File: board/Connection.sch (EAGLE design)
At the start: 44 parts, among them U2 SN65HVD230, U5 ADA4528-1ARMZ-R7, X1 MKDSN1,5/4-5,08

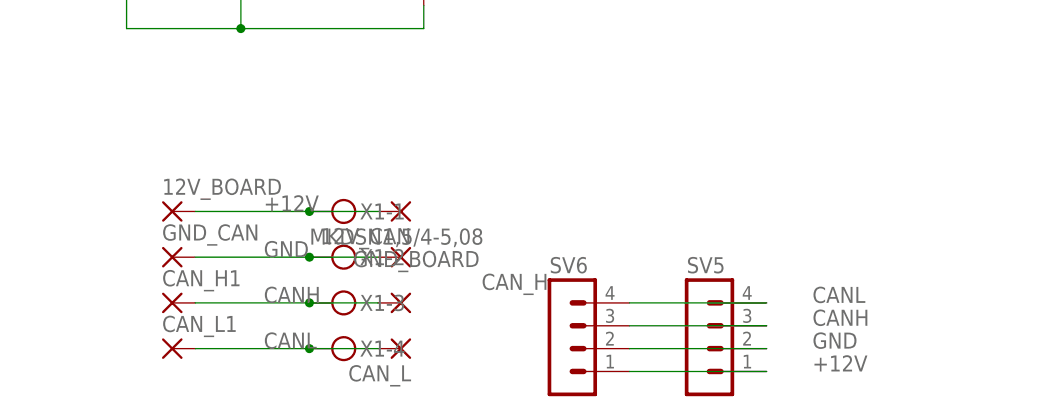
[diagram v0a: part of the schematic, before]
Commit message: Used power terminal
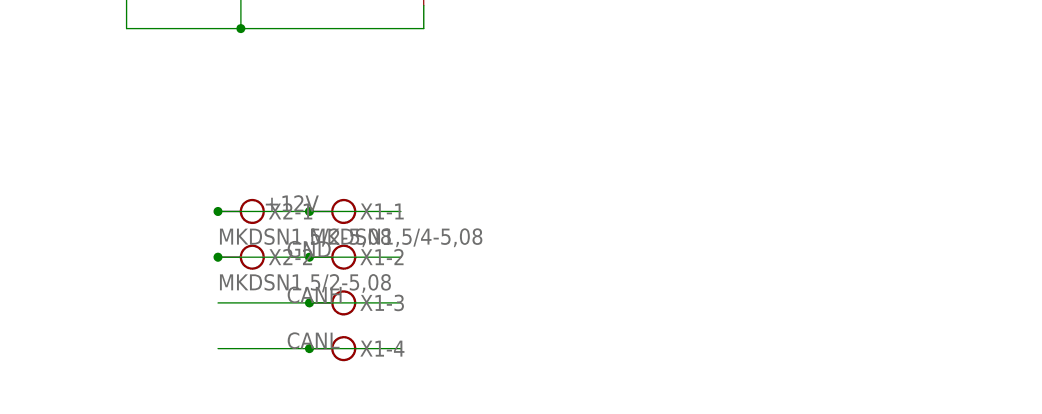
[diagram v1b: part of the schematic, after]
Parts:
- removed 12V_BOARD, 12V_CAN: 12V, wirepad:1,6/0,8
- removed CAN_H, CAN_H1, CAN_L, CAN_L1, GND_BOARD, GND_CAN: (no value), wirepad:1,6/0,8
- removed SV5, SV6: (no value), con-lstb:MA04-1
- added X2: MKDSN1,5/2-5,08, con-phoenix-508:MKDSN1,5/2-5,08
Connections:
- net +12V: now also X2-1.KL; no longer 12V_BOARD.P, 12V_CAN.P, SV5.1, SV6.1
- net CANH: no longer CAN_H.P, CAN_H1.P, SV5.3, SV6.3
- net CANL: no longer CAN_L.P, CAN_L1.P, SV5.4, SV6.4
- net GND: now also X2-2.KL; no longer GND_BOARD.P, GND_CAN.P, SV5.2, SV6.2

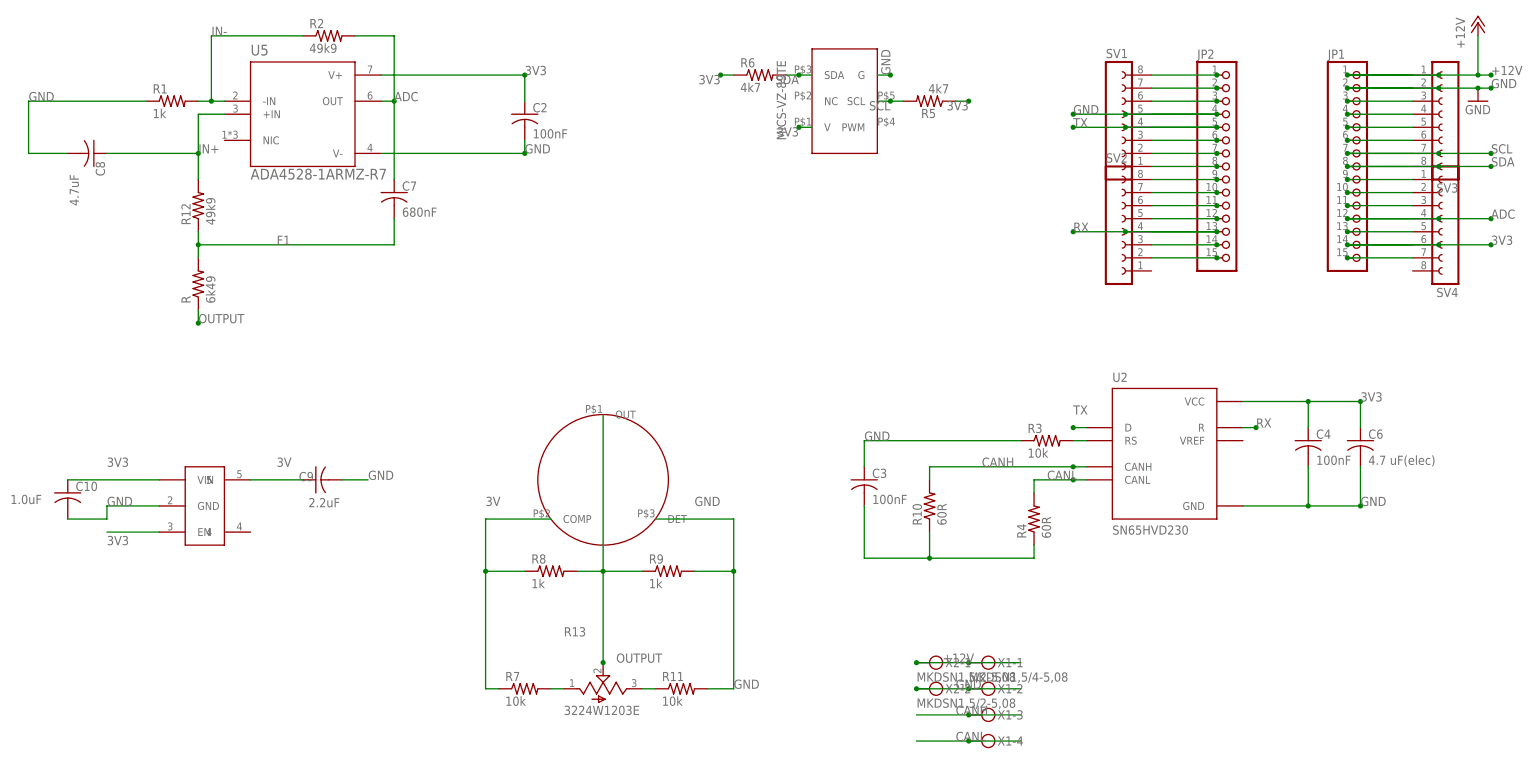
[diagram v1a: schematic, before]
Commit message: Optimized the size of PCB
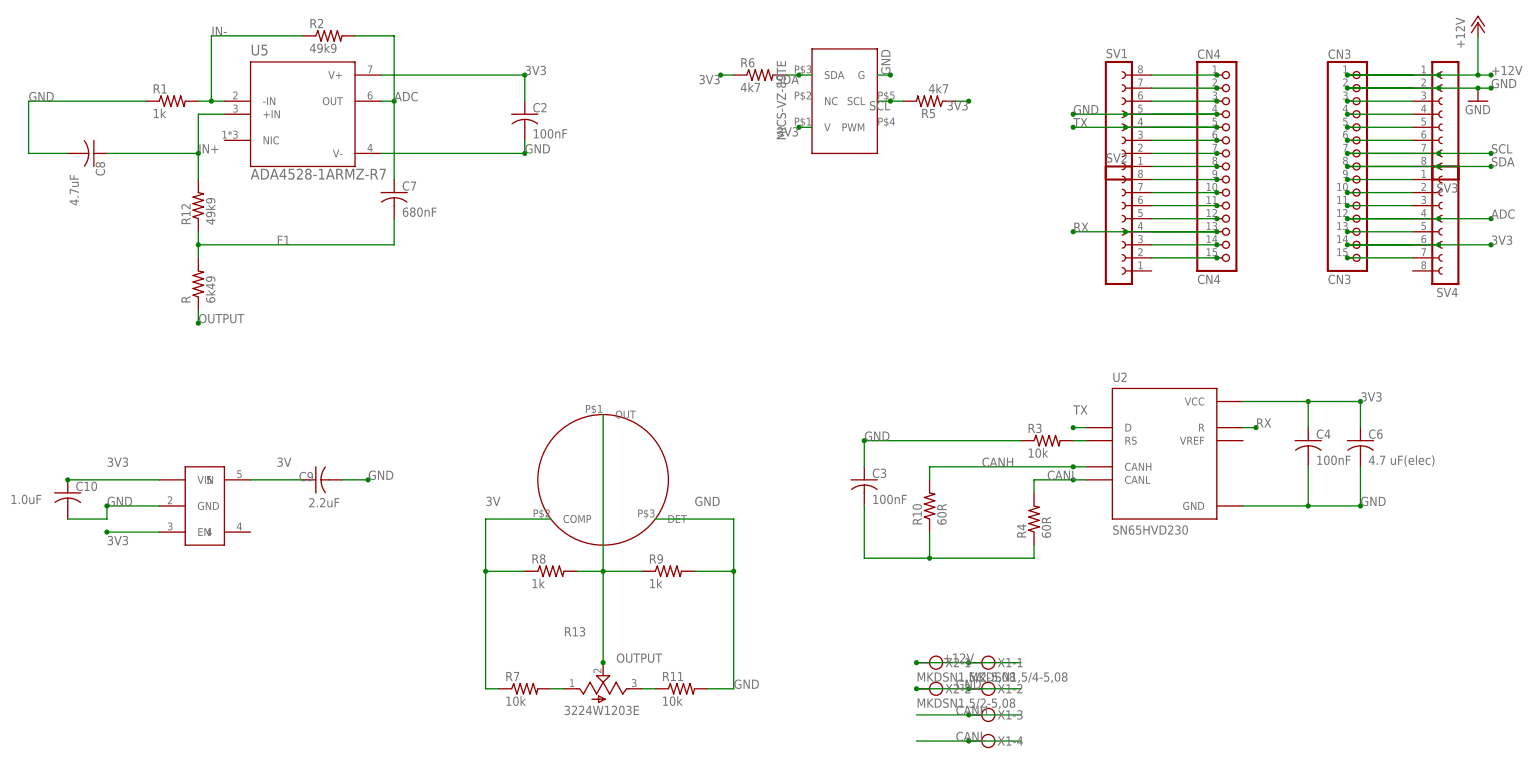
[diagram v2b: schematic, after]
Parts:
- CN3: value (none) -> CN3
- CN4: value (none) -> CN4
- renumbered JP1 to CN3, JP2 to CN4

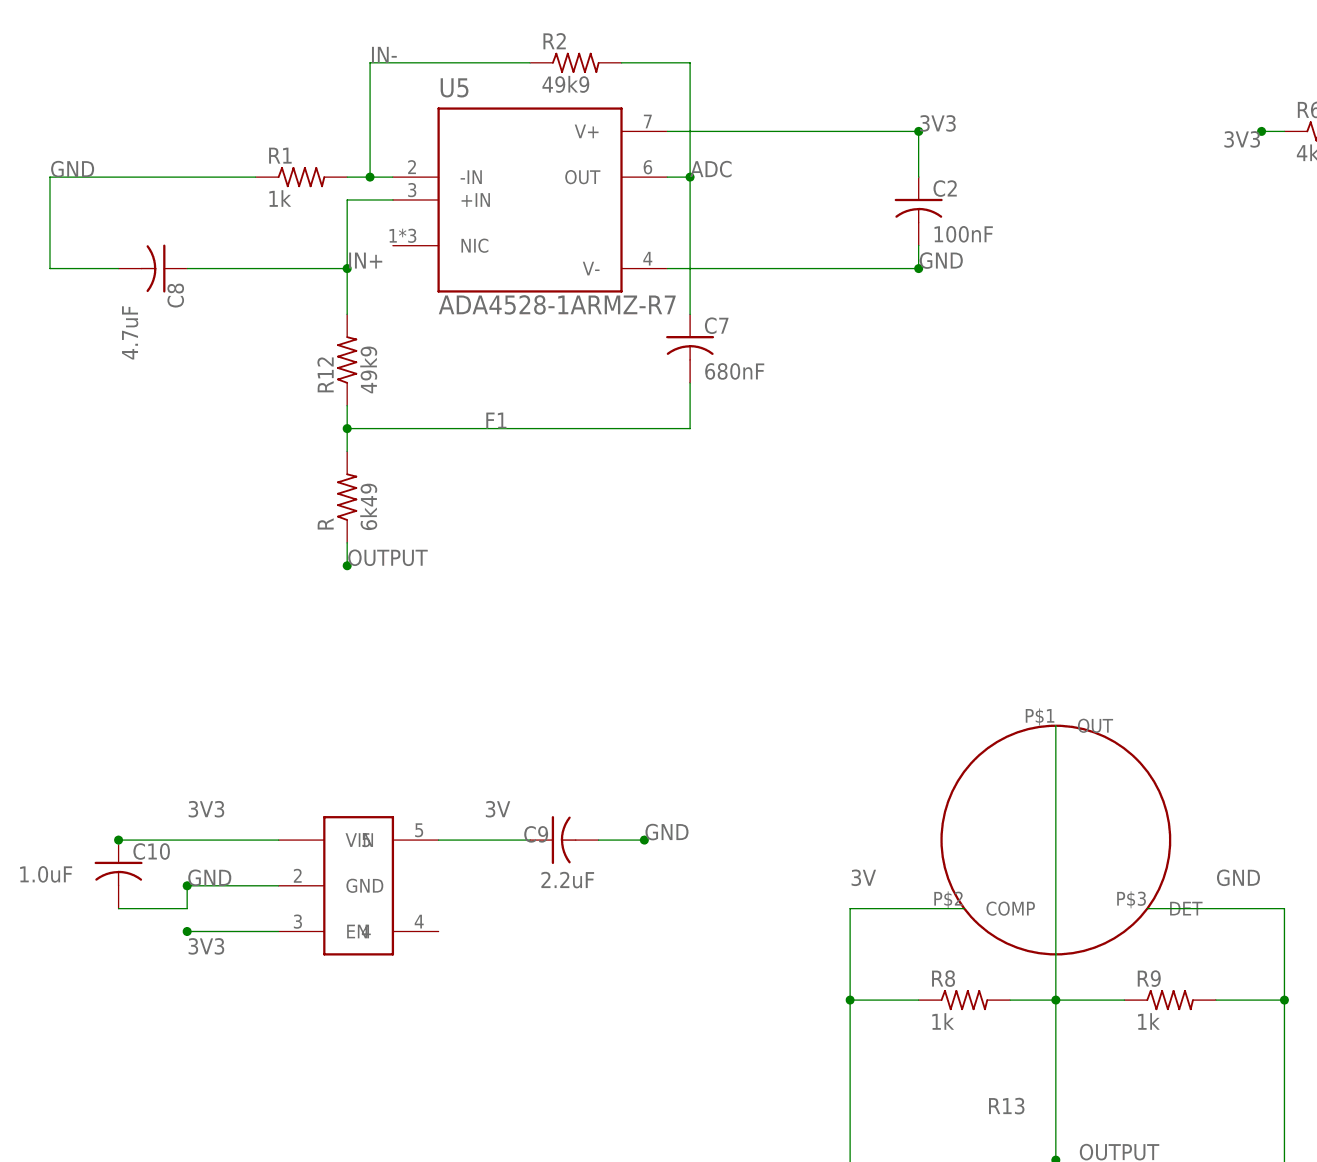
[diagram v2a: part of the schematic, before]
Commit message: Updated the design according to the real connection.
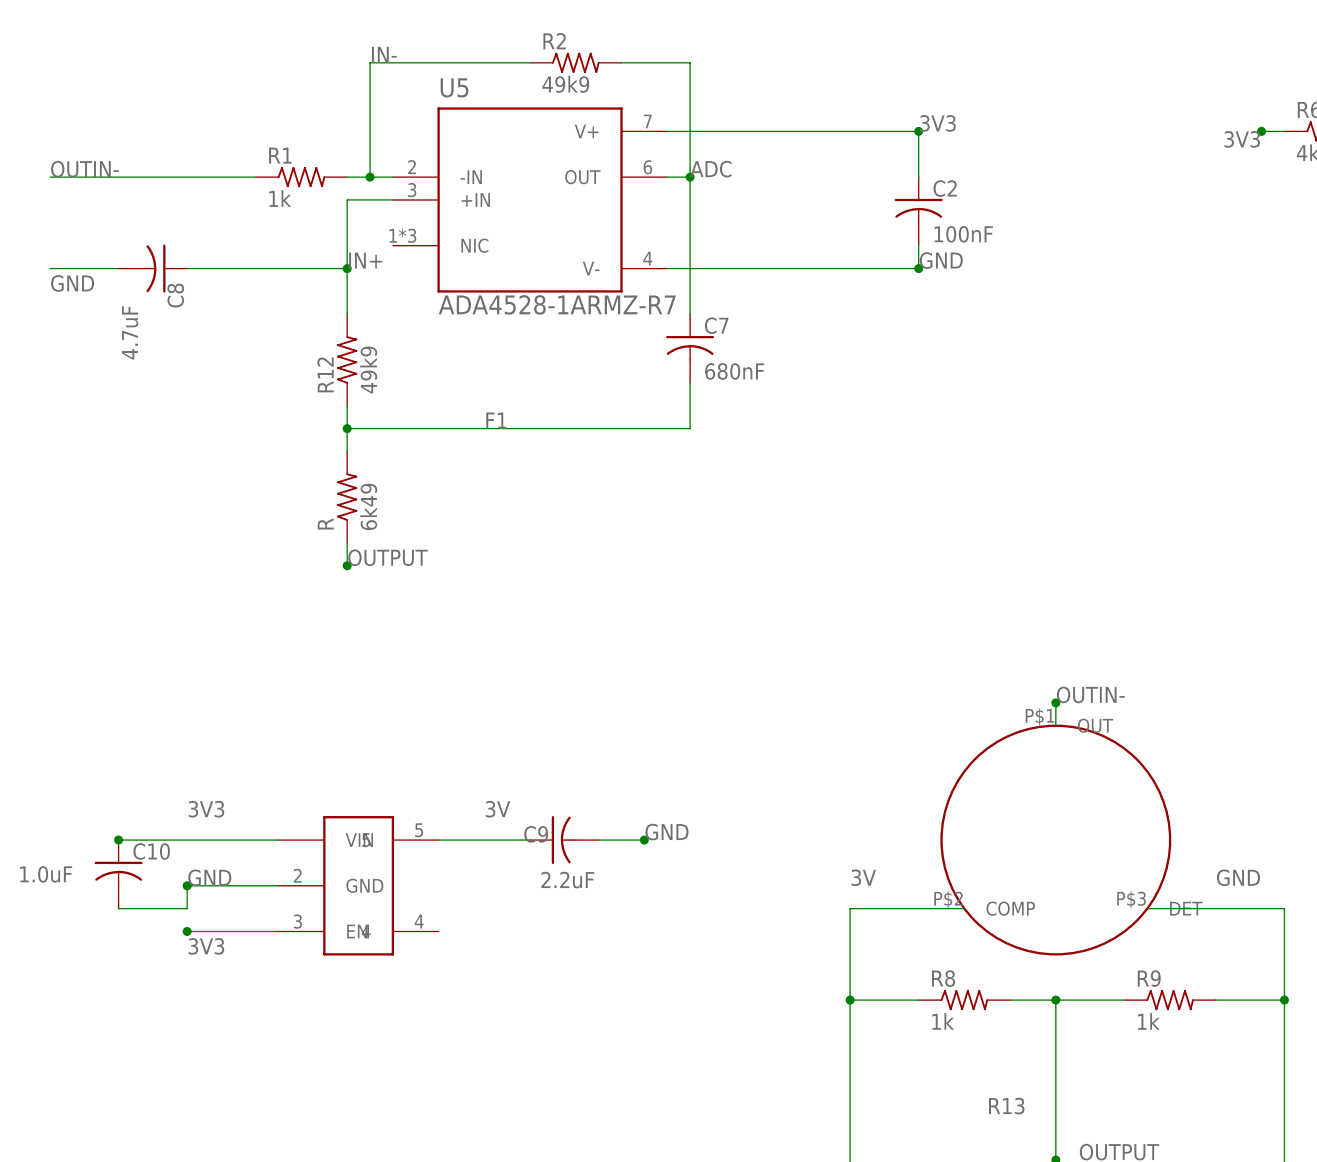
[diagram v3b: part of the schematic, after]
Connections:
- new net OUTIN-: R1.1, U$1.OUT
- net GND: no longer R1.1
- net OUTPUT: no longer U$1.OUT
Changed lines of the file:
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@@
-</segment>
-<segment>
-<pinref part="R1" gate="G$1" pin="1"/>
-<wire x1="7.62" y1="93.98" x2="-15.24" y2="93.98" width="0.1524" layer="91" grouprefs="AMP_WITH_FILTER"/>
-<pinref part="C8" gate="G$1" pin="2"/>
-<wire x1="-7.62" y1="83.82" x2="-15.24" y2="83.82" width="0.1524" layer="91" grouprefs="AMP_WITH_FILTER"/>
-<wire x1="-15.24" y1="83.82" x2="-15.24" y2="93.98" width="0.1524" layer="91" grouprefs="AMP_WITH_FILTER"/>
-<label x="-15.24" y="93.98" size="1.778" layer="95" grouprefs="AMP_WITH_FILTER"/>
 </segment>
 <segment>
@@
 <wire x1="215.9" y1="91.44" x2="203.2" y2="91.44" width="0.1524" layer="91"/>
 </segment>
+<segment>
+<pinref part="C8" gate="G$1" pin="2"/>
+<wire x1="-7.62" y1="83.82" x2="-15.24" y2="83.82" width="0.1524" layer="91" grouprefs="AMP_WITH_FILTER"/>
+<label x="-15.24" y="81.28" size="1.778" layer="95"/>
+</segment>
 </net>
 <net name="TX" class="0">
@@
 <junction x="96.52" y="-15.24" grouprefs="MP7227"/>
 <label x="99.06" y="-15.24" size="1.778" layer="95" grouprefs="MP7227"/>
-<pinref part="U$1" gate="G$1" pin="OUT"/>
-<wire x1="96.52" y1="2.54" x2="96.52" y2="33.02" width="0.1524" layer="91" grouprefs="MP7227"/>
 </segment>
 <segment>
@@
 </segment>
 </net>
+<net name="OUTIN-" class="0">
+<segment>
+<pinref part="R1" gate="G$1" pin="1"/>
+<wire x1="7.62" y1="93.98" x2="-15.24" y2="93.98" width="0.1524" layer="91" grouprefs="AMP_WITH_FILTER"/>
+<label x="-15.24" y="93.98" size="1.778" layer="95" grouprefs="AMP_WITH_FILTER"/>
+</segment>
+<segment>
+<pinref part="U$1" gate="G$1" pin="OUT"/>
+<wire x1="96.52" y1="33.02" x2="96.52" y2="35.56" width="0.1524" layer="91"/>
+<junction x="96.52" y="35.56"/>
+<label x="96.52" y="35.56" size="1.778" layer="95"/>
+</segment>
+</net>
